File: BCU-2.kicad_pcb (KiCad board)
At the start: 2 copper layers, 106 x 91.4 mm, 92 parts, among them J1 Screw_Terminal_01x04, J2 Conn_01x12_Male, J3 Screw_Terminal_01x04, J4 Conn_01x05_Male, J5 Conn_01x05_Male, J6 Conn_01x04_Male, J7 Conn_01x04_Male, Q1 2N7002, Q2 NTF6P02, Q3 2N7002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

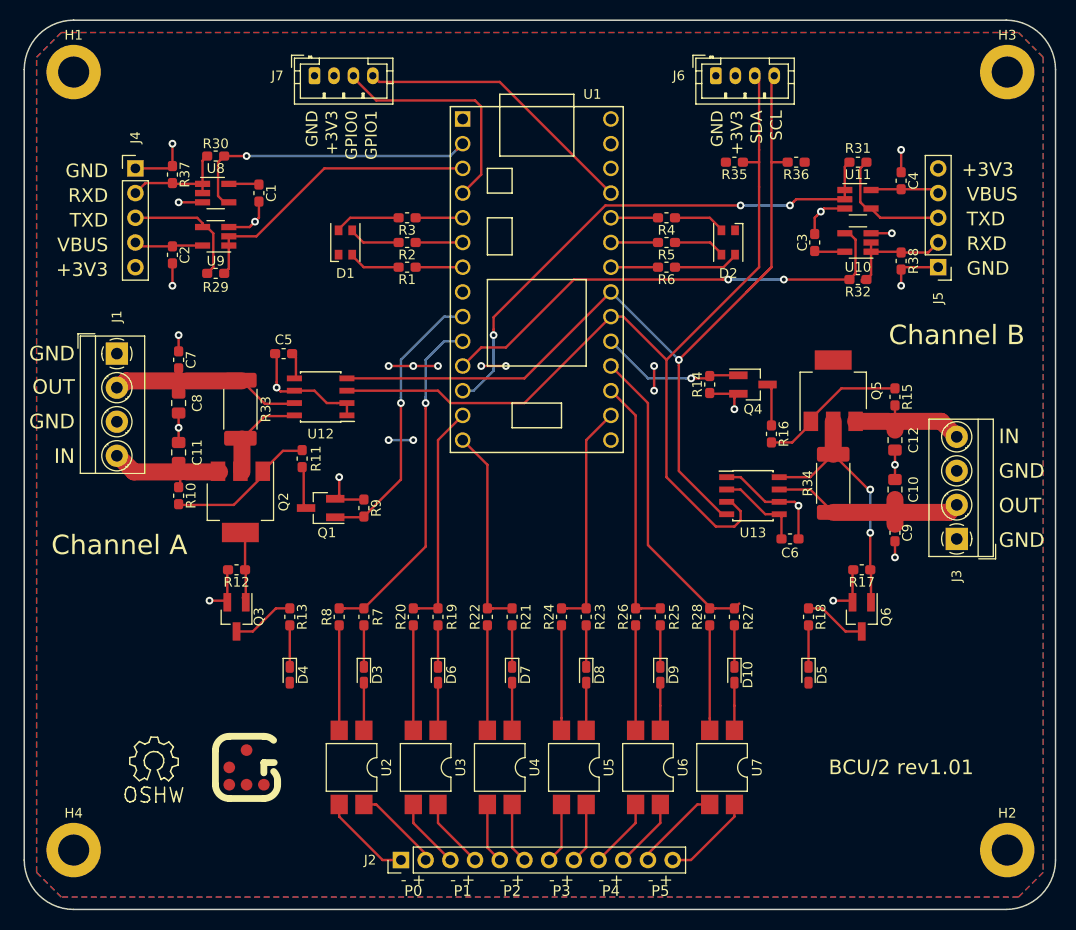
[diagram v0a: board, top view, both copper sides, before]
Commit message: Update to KiCad 6
Signed-off-by: Geert Uytterhoeven <geert@linux-m68k.org>
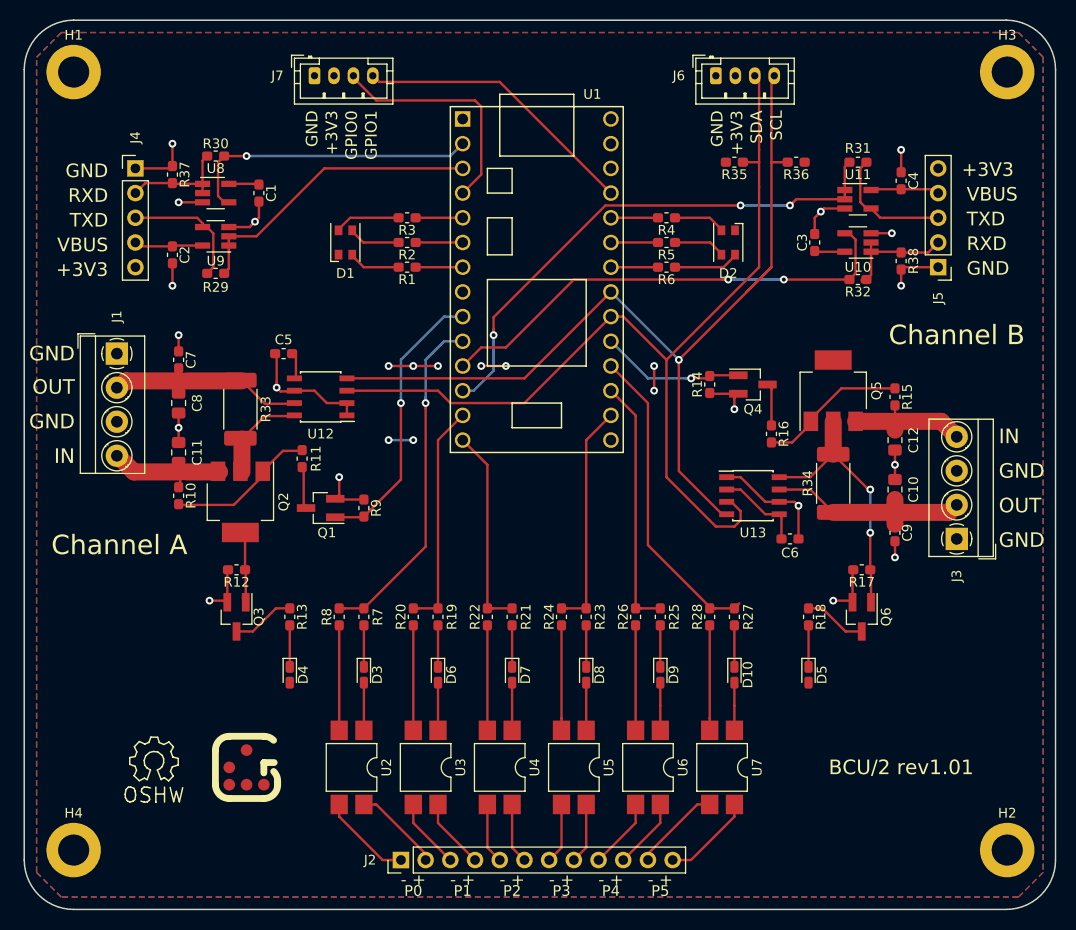
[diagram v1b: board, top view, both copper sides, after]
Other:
- net class Default removed
